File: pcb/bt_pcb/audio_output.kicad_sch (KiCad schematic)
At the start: 37 parts, among them J17 ReanNYS216G, J18 ReanNYS216G, U3 MCP6004

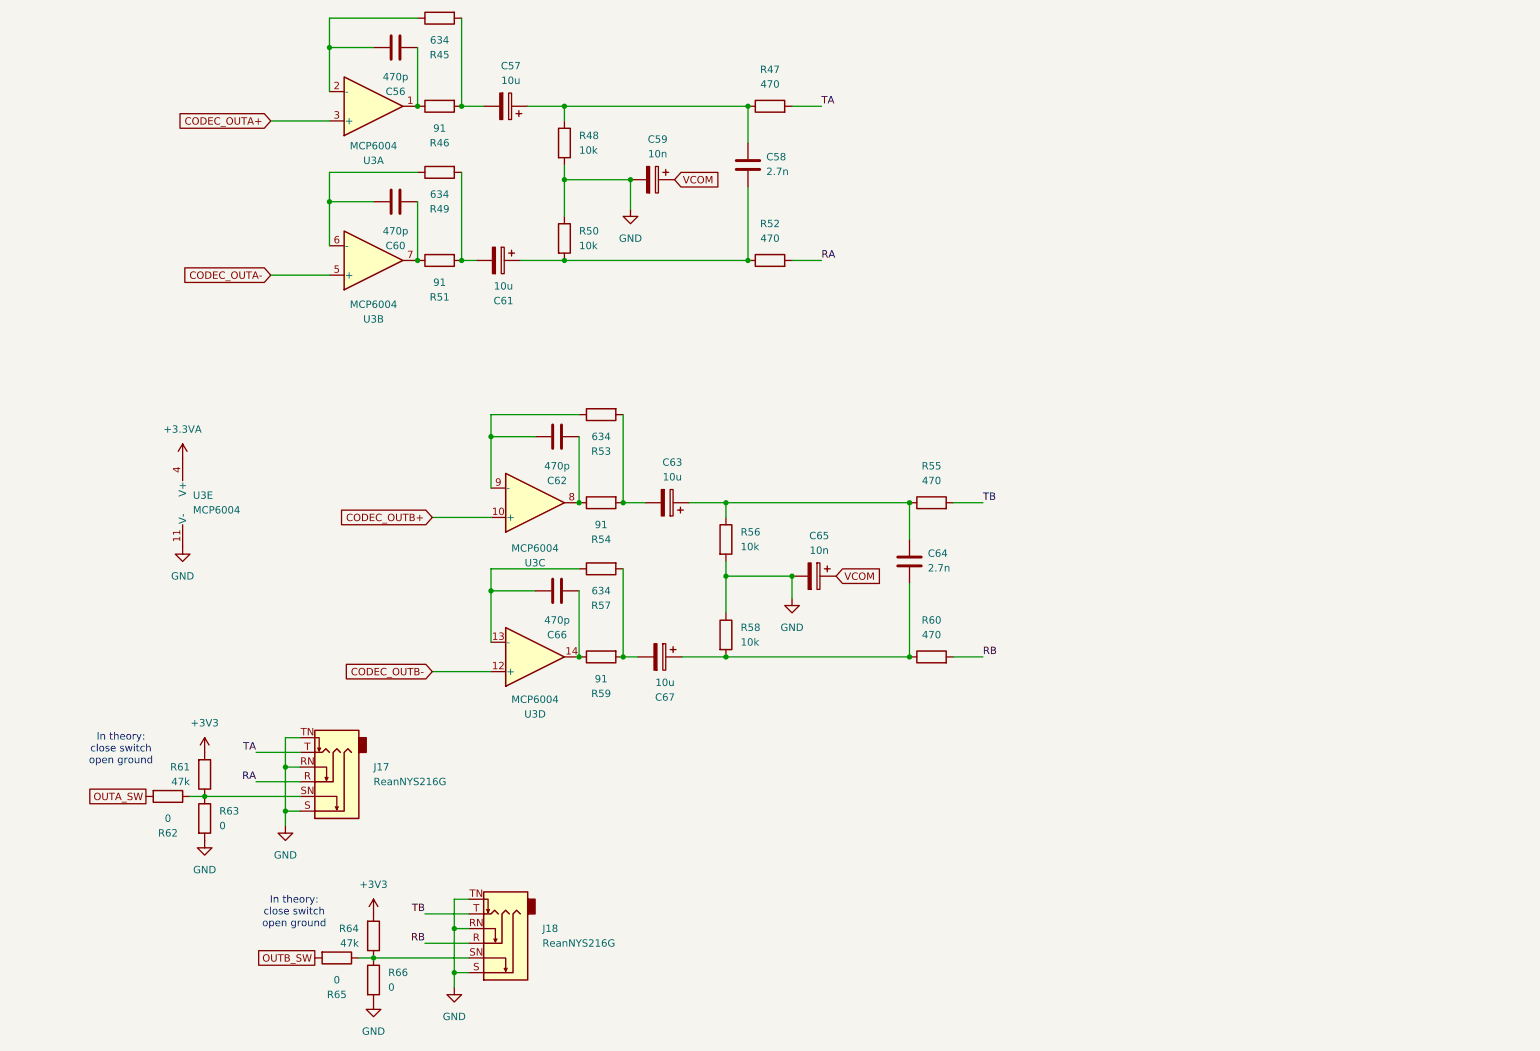
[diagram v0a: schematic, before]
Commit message: doing pcb from scratch again
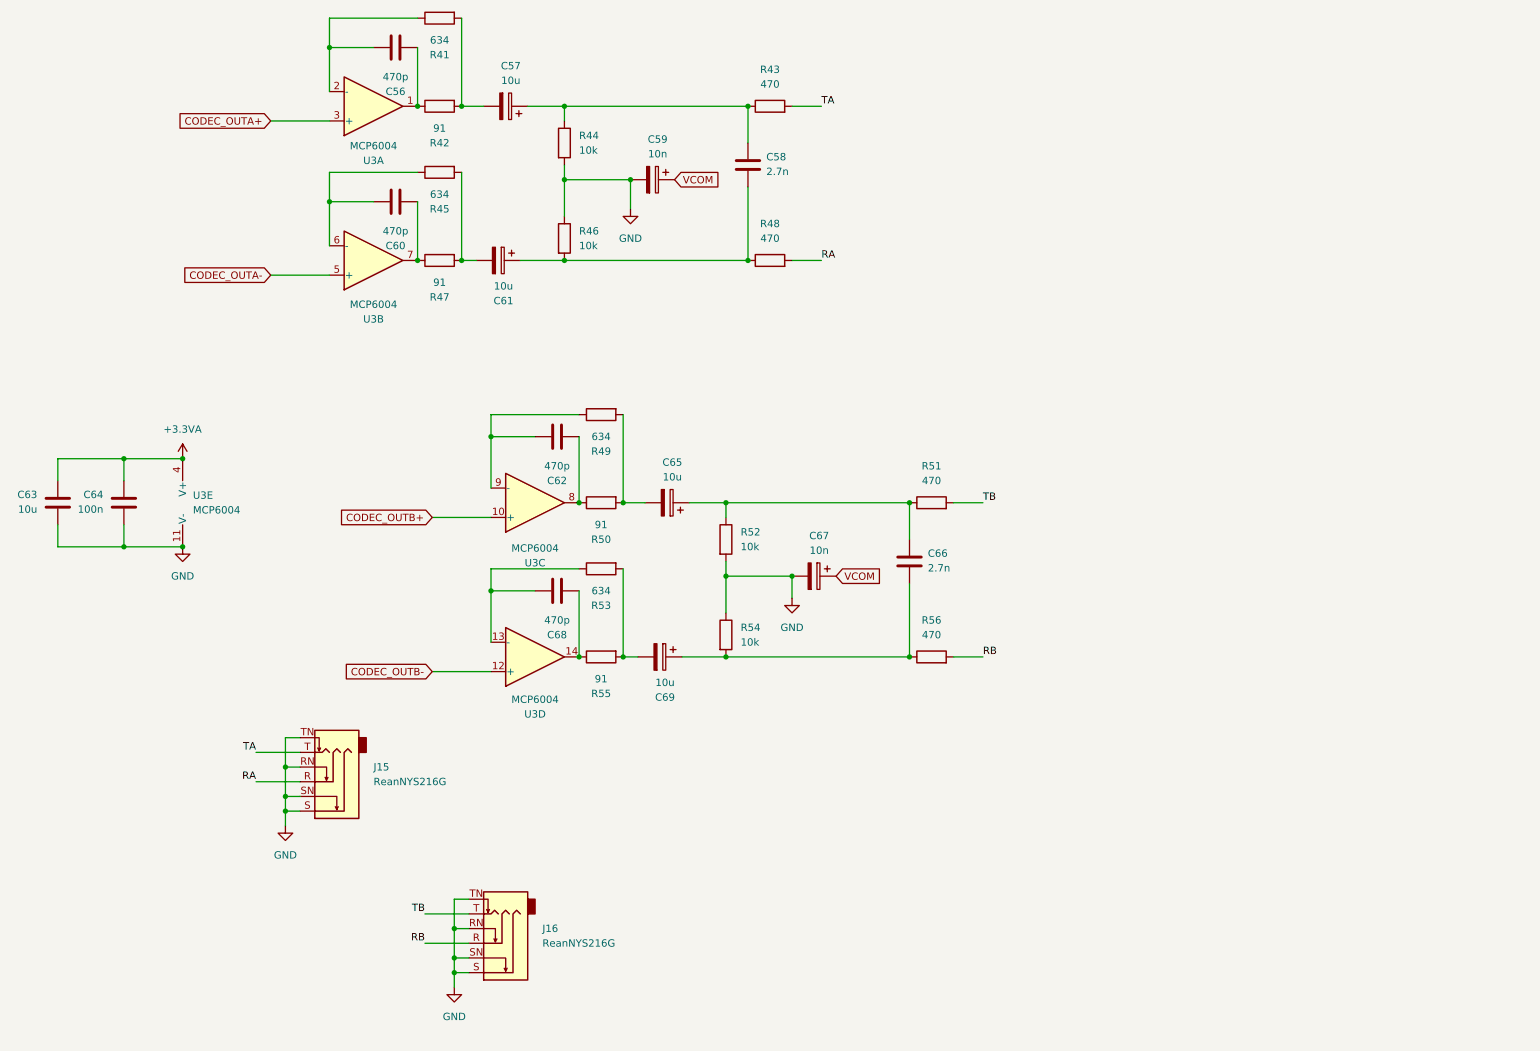
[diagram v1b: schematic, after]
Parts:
- removed R61, R64: 47k, Resistor_SMD:R_0603_1608Metric_Pad0.98x0.95mm_HandSolder, symbol Device:R
- removed R62, R63, R65, R66: 0, Resistor_SMD:R_0603_1608Metric_Pad0.98x0.95mm_HandSolder, symbol Device:R
- added C63: 10u, Capacitor_SMD:C_0603_1608Metric_Pad1.08x0.95mm_HandSolder, symbol Device:C
- added C64: 100n, Capacitor_SMD:C_0603_1608Metric_Pad1.08x0.95mm_HandSolder, symbol Device:C
- renumbered C63 to C65, C64 to C66, C65 to C67, C66 to C68, C67 to C69, J17 to J15, J18 to J16, R45 to R41, R46 to R42, R47 to R43, R48 to R44, R49 to R45, R50 to R46, R51 to R47, R52 to R48, R53 to R49, R54 to R50, R55 to R51, R56 to R52, R57 to R53, R58 to R54, R59 to R55, R60 to R56
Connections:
- net +3.3VA: now also C63.1, C64.1
- net GND: now also J15.SN, J16.SN, C63.2, C64.2
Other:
- note removed: "In theory: close switch open ground"

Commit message: redo of power supply
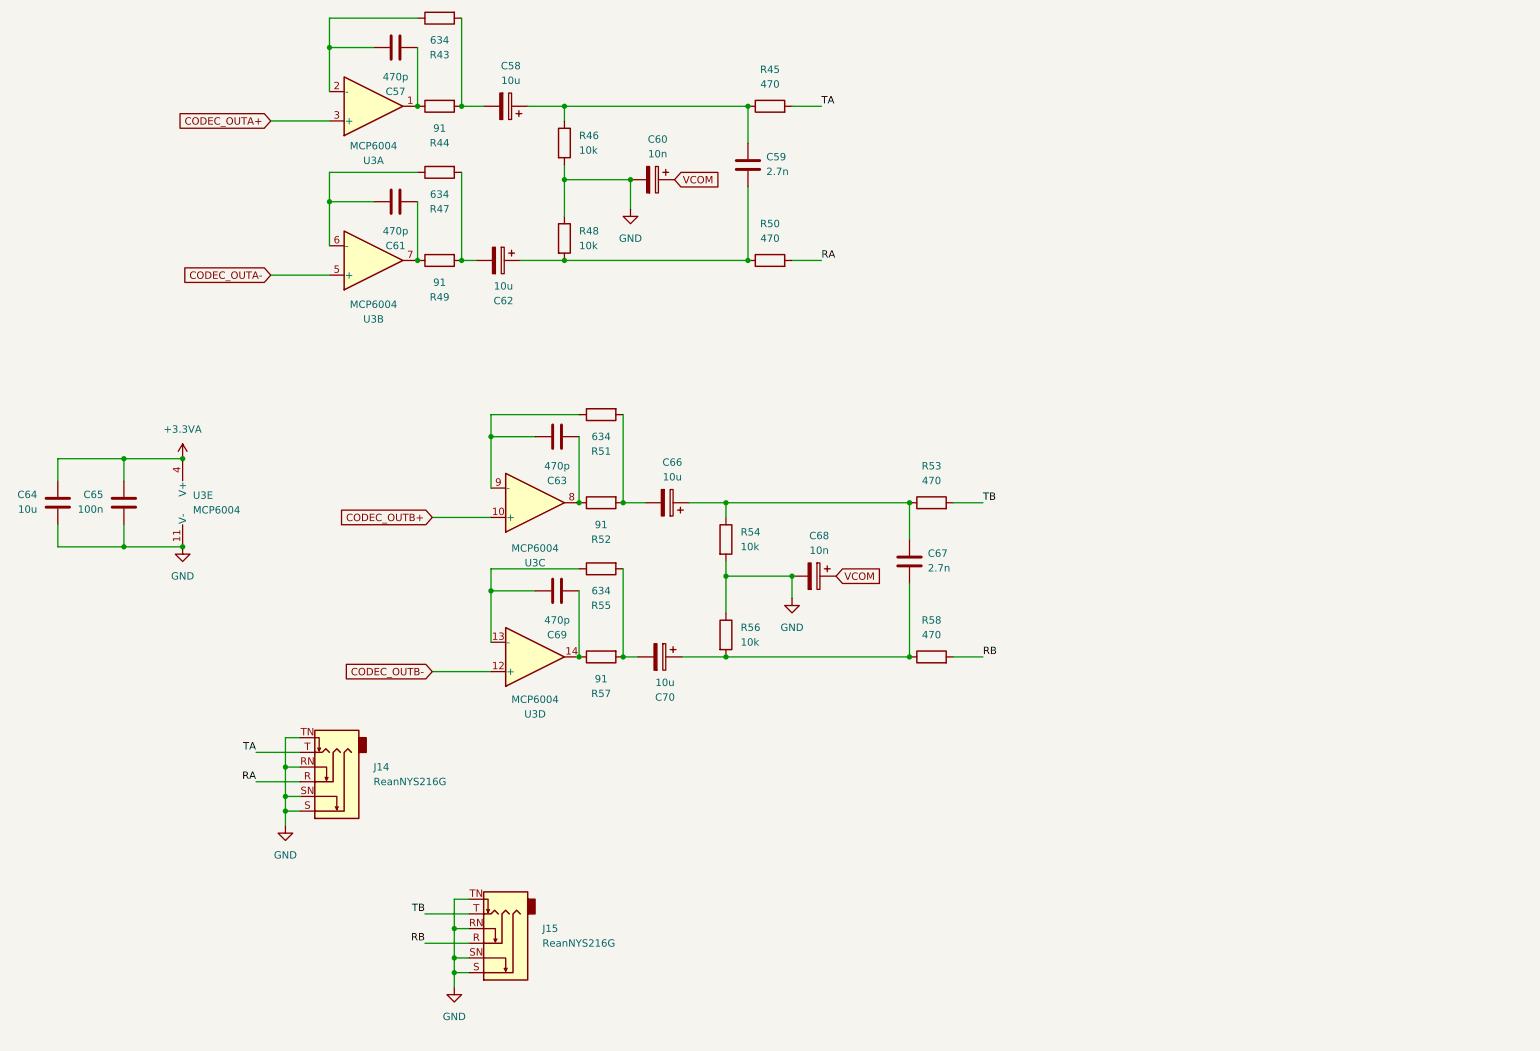
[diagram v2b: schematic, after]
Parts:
- renumbered C56 to C57, C57 to C58, C58 to C59, C59 to C60, C60 to C61, C61 to C62, C62 to C63, C63 to C64, C64 to C65, C65 to C66, C66 to C67, C67 to C68, C68 to C69, C69 to C70, J15 to J14, J16 to J15, R41 to R43, R42 to R44, R43 to R45, R44 to R46, R45 to R47, R46 to R48, R47 to R49, R48 to R50, R49 to R51, R50 to R52, R51 to R53, R52 to R54, R53 to R55, R54 to R56, R55 to R57, R56 to R58

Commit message: made a bom
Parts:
- C64: footprint Capacitor_SMD:C_0603_1608Metric_Pad1.08x0.95mm_HandSolder -> Capacitor_SMD:C_0805_2012Metric_Pad1.18x1.45mm_HandSolder

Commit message: seeing the end of the tunnel
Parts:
- J15: renamed from J14; now not fitted
- J16: renamed from J15; now not fitted
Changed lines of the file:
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@@
 			)
 		)
-		(property "Description" ""
+		(property "Description" "AUDIO"
 			(at 97.79 31.75 0)
 			(effects
@@
 					(size 1.27 1.27)
 				)
+				(hide yes)
 			)
 		)
@@
 			)
 		)
-		(property "Description" ""
+		(property "Description" "AUDIO"
 			(at 167.64 110.49 0)
 			(effects
@@
 					(size 1.27 1.27)
 				)
+				(hide yes)
 			)
 		)
@@
 		(in_bom yes)
 		(on_board yes)
-		(dnp no)
+		(dnp yes)
 		(fields_autoplaced yes)
-		(property "Reference" "J15"
+		(property "Reference" "J16"
 			(at 104.14 173.9899 0)
 			(effects
@@
 			(project "bt_pcb"
 				(path "/eb787481-08cd-41a4-a128-173fa6227c32/4ada0139-8712-47ce-9d4c-ab8fef312f7b/92a88d42-e0ca-481e-a77e-2117fd7dfc0f"
-					(reference "J15")
+					(reference "J16")
 					(unit 1)
 				)
@@
 			)
 		)
-		(property "Description" ""
+		(property "Description" "AUDIO"
 			(at 106.68 88.9 0)
 			(effects
@@
 					(size 1.27 1.27)
 				)
+				(hide yes)
 			)
 		)
@@
 			)
 		)
-		(property "Description" ""
+		(property "Description" "AUDIO"
 			(at 123.19 44.45 0)
 			(effects
@@
 					(size 1.27 1.27)
 				)
+				(hide yes)
 			)
 		)
@@
 			)
 		)
-		(property "Description" ""
+		(property "Description" "AUDIO"
 			(at 106.68 115.57 0)
 			(effects
@@
 					(size 1.27 1.27)
 				)
+				(hide yes)
 			)
 		)
@@
 			)
 		)
-		(property "Description" ""
+		(property "Description" "AUDIO"
 			(at 124.46 127 0)
 			(effects
@@
 					(size 1.27 1.27)
 				)
+				(hide yes)
 			)
 		)
@@
 		(dnp no)
 		(fields_autoplaced yes)
-		(property "Reference" "#PWR0134"
+		(property "Reference" "#PWR0135"
 			(at 147.32 123.19 0)
 			(effects
@@
 			(project "bt_pcb"
 				(path "/eb787481-08cd-41a4-a128-173fa6227c32/4ada0139-8712-47ce-9d4c-ab8fef312f7b/92a88d42-e0ca-481e-a77e-2117fd7dfc0f"
-					(reference "#PWR0134")
+					(reference "#PWR0135")
 					(unit 1)
 				)
@@
 			)
 		)
-		(property "Description" ""
+		(property "Description" "AUDIO"
 			(at 78.74 21.59 0)
 			(effects
@@
 					(size 1.27 1.27)
 				)
+				(hide yes)
 			)
 		)
@@
 			)
 		)
-		(property "Description" ""
+		(property "Description" "AUDIO"
 			(at 78.74 48.26 0)
 			(effects
@@
 					(size 1.27 1.27)
 				)
+				(hide yes)
 			)
 		)
@@
 			)
 		)
-		(property "Description" ""
+		(property "Description" "APD"
 			(at 31.75 100.33 0)
 			(effects
@@
 					(size 1.27 1.27)
 				)
+				(hide yes)
 			)
 		)
@@
 		(dnp no)
 		(fields_autoplaced yes)
-		(property "Reference" "#PWR0136"
+		(property "Reference" "#PWR0137"
 			(at 88.9 190.5 0)
 			(effects
@@
 			(project "bt_pcb"
 				(path "/eb787481-08cd-41a4-a128-173fa6227c32/4ada0139-8712-47ce-9d4c-ab8fef312f7b/92a88d42-e0ca-481e-a77e-2117fd7dfc0f"
-					(reference "#PWR0136")
+					(reference "#PWR0137")
 					(unit 1)
 				)
@@
 			)
 		)
-		(property "Description" ""
+		(property "Description" "AUDIO"
 			(at 151.13 113.03 0)
 			(effects
@@
 					(size 1.27 1.27)
 				)
+				(hide yes)
 			)
 		)
@@
 			)
 		)
-		(property "Description" ""
+		(property "Description" "APD"
 			(at 20.32 100.33 0)
 			(effects
@@
 					(size 1.27 1.27)
 				)
+				(hide yes)
 			)
 		)
@@
 		(on_board yes)
 		(dnp no)
-		(property "Reference" "#PWR0133"
+		(property "Reference" "#PWR0134"
 			(at 41.91 114.3 0)
 			(effects
@@
 			(project "bt_pcb"
 				(path "/eb787481-08cd-41a4-a128-173fa6227c32/4ada0139-8712-47ce-9d4c-ab8fef312f7b/92a88d42-e0ca-481e-a77e-2117fd7dfc0f"
-					(reference "#PWR0133")
+					(reference "#PWR0134")
 					(unit 1)
 				)
@@
 		(dnp no)
 		(fields_autoplaced yes)
-		(property "Reference" "#PWR0131"
+		(property "Reference" "#PWR0132"
 			(at 119.38 55.88 0)
 			(effects
@@
 			(project "bt_pcb"
 				(path "/eb787481-08cd-41a4-a128-173fa6227c32/4ada0139-8712-47ce-9d4c-ab8fef312f7b/92a88d42-e0ca-481e-a77e-2117fd7dfc0f"
-					(reference "#PWR0131")
+					(reference "#PWR0132")
 					(unit 1)
 				)
@@
 			)
 		)
-		(property "Description" ""
+		(property "Description" "AUDIO"
 			(at 139.7 41.91 0)
 			(effects
@@
 					(size 1.27 1.27)
 				)
+				(hide yes)
 			)
 		)
@@
 		(in_bom yes)
 		(on_board yes)
-		(dnp no)
+		(dnp yes)
 		(fields_autoplaced yes)
-		(property "Reference" "J14"
+		(property "Reference" "J15"
 			(at 74.93 146.05 0)
 			(effects
@@
 			(project "bt_pcb"
 				(path "/eb787481-08cd-41a4-a128-173fa6227c32/4ada0139-8712-47ce-9d4c-ab8fef312f7b/92a88d42-e0ca-481e-a77e-2117fd7dfc0f"
-					(reference "J14")
+					(reference "J15")
 					(unit 1)
 				)
@@
 			)
 		)
-		(property "Description" ""
+		(property "Description" "AUDIO"
 			(at 125.73 100.33 0)
 			(effects
@@
 					(size 1.27 1.27)
 				)
+				(hide yes)
 			)
 		)
@@
 		(dnp no)
 		(fields_autoplaced yes)
-		(property "Reference" "#PWR0132"
+		(property "Reference" "#PWR0133"
 			(at 41.91 96.52 0)
 			(effects
@@
 			(project "bt_pcb"
 				(path "/eb787481-08cd-41a4-a128-173fa6227c32/4ada0139-8712-47ce-9d4c-ab8fef312f7b/92a88d42-e0ca-481e-a77e-2117fd7dfc0f"
-					(reference "#PWR0132")
+					(reference "#PWR0133")
 					(unit 1)
 				)
@@
 			)
 		)
-		(property "Description" ""
+		(property "Description" "AUDIO"
 			(at 96.52 58.42 0)
 			(effects
@@
 					(size 1.27 1.27)
 				)
+				(hide yes)
 			)
 		)
@@
 		(dnp no)
 		(fields_autoplaced yes)
-		(property "Reference" "#PWR0135"
+		(property "Reference" "#PWR0136"
 			(at 59.69 162.56 0)
 			(effects
@@
 			(project "bt_pcb"
 				(path "/eb787481-08cd-41a4-a128-173fa6227c32/4ada0139-8712-47ce-9d4c-ab8fef312f7b/92a88d42-e0ca-481e-a77e-2117fd7dfc0f"
-					(reference "#PWR0135")
+					(reference "#PWR0136")
 					(unit 1)
 				)

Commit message: aaaaaaa
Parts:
- added J15: Conn_01x03, Connector_JST:JST_PH_B3B-PH-K_1x03_P2.00mm_Vertical, symbol Connector_Generic:Conn_01x03
- J13: renamed from J15; now fitted
- J14: renamed from J16; now fitted
- renumbered C57 to C66, C61 to C67, C62 to C68, C58 to C69, C63 to C70, C69 to C71, C60 to C72, C70 to C73, C66 to C74, C59 to C75, C68 to C76, C67 to C77, R43 to R40, R44 to R41, R47 to R42, R49 to R43, R46 to R44, R48 to R45, R51 to R46, R52 to R47, R55 to R48, R57 to R49, R54 to R50, R56 to R51, R45 to R52, R50 to R53, R53 to R54, R58 to R55
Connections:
- net VCOM renamed OUT_VMID
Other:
- note added: "HEADPHONE OUT Left -> 1 -> T Right -> 2 -> R Ggn -> 3 -> S"

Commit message: schematic rev b finish?
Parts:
- removed J15: Conn_01x03, Connector_JST:JST_PH_B3B-PH-K_1x03_P2.00mm_Vertical, symbol Connector_Generic:Conn_01x03
- renumbered C66 to C79, C69 to C80, C75 to C81, C72 to C82, C67 to C83, C68 to C84, C70 to C85, C64 to C86, C65 to C87, C74 to C88, C77 to C89, C76 to C90, C71 to C91, C73 to C92, J13 to J14, J14 to J15, R40 to R41, R41 to R42, R52 to R43, R42 to R45, R45 to R46, R43 to R47, R53 to R48, R46 to R49, R47 to R50, R54 to R51, R50 to R52, R48 to R53, R51 to R54, R49 to R55, R55 to R56, U3 to U4
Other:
- note removed: "HEADPHONE OUT Left -> 1 -> T Right -> 2 -> R Ggn -> 3 -> S"
- moved on the sheet: C82, C90

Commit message: just need to fix usb
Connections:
- net CODEC_OUTB+: now also U4.12 (+); no longer U4.10 (+)
- net CODEC_OUTB-: now also U4.10 (+); no longer U4.12 (+)
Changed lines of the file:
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@@
 		)
 	)
-	(global_label "CODEC_OUTA-"
+	(global_label "CODEC_OUTB+"
 		(shape input)
-		(at 57.15 60.96 180)
+		(at 85.09 129.54 180)
 		(fields_autoplaced yes)
 		(effects
@@
 		)
 		(property "Intersheetrefs" "${INTERSHEET_REFS}"
-			(at 40.6181 60.96 0)
+			(at 68.3767 129.54 0)
 			(hide yes)
 			(show_name no)
@@
 		)
 	)
-	(global_label "CODEC_OUTB+"
+	(global_label "CODEC_OUTB-"
 		(shape input)
 		(at 85.09 102.87 180)
@@
 		)
 	)
-	(global_label "CODEC_OUTB-"
+	(global_label "CODEC_OUTA-"
 		(shape input)
-		(at 85.09 129.54 180)
+		(at 57.15 60.96 180)
 		(fields_autoplaced yes)
 		(effects
@@
 		)
 		(property "Intersheetrefs" "${INTERSHEET_REFS}"
-			(at 68.3767 129.54 0)
+			(at 40.6181 60.96 0)
 			(hide yes)
 			(show_name no)

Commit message: sd kind of in
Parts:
- renumbered C79 to C80, C80 to C81, C81 to C82, C82 to C83, C83 to C84, C84 to C85, C85 to C86, C86 to C87, C87 to C88, C88 to C89, C89 to C90, C90 to C91, C91 to C92, C92 to C93, J14 to J15, J15 to J16, R41 to R39, R42 to R40, R43 to R41, R44 to R42, R45 to R43, R46 to R44, R47 to R45, R48 to R46, R49 to R47, R50 to R48, R51 to R49, R52 to R50, R53 to R51, R54 to R52, R55 to R53, R56 to R54
